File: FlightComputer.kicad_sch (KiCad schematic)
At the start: 0 parts

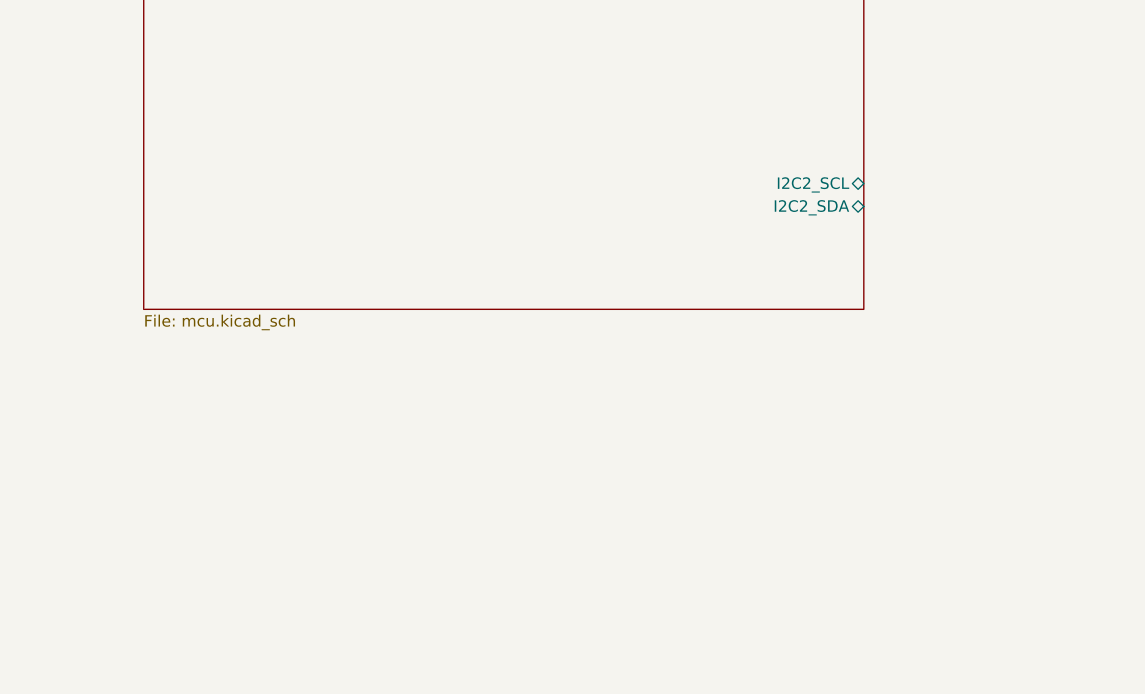
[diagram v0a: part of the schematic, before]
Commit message: Add NavBoard connector and fix Ferrite bead for 3V3A line
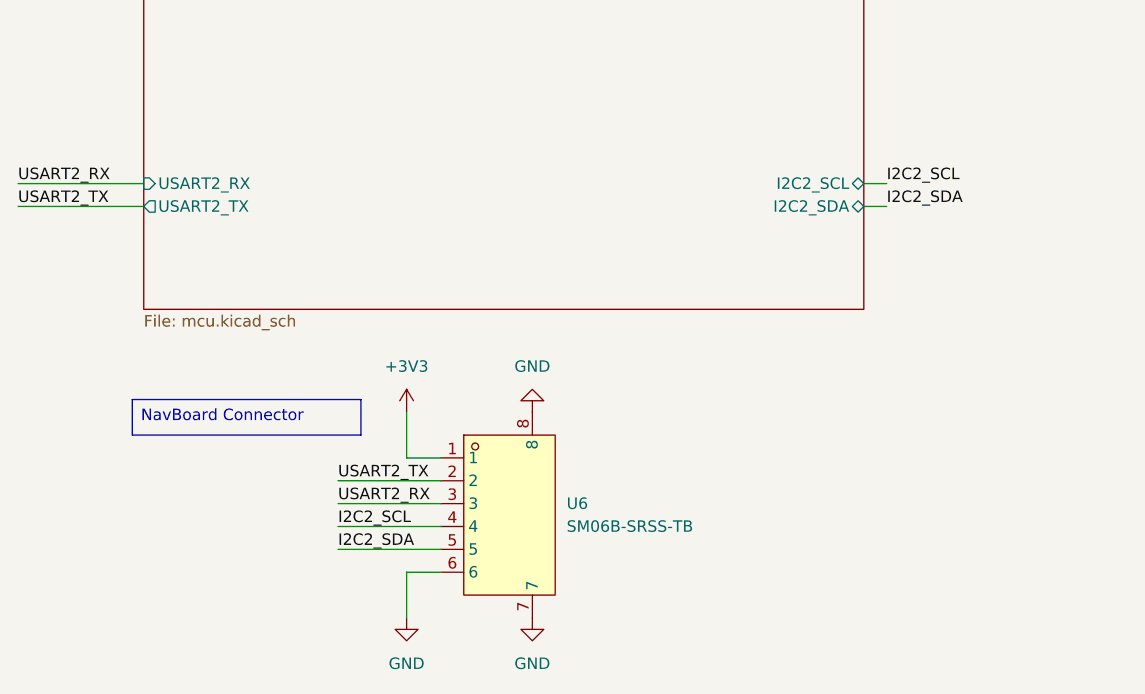
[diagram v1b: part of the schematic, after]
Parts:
- added U6: SM06B-SRSS-TB, LCSC:CONN-SMD_SM06B-SRSS-TB-LF-SN, symbol LCSC:SM06B-SRSS-TB
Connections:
- new net +3V3: U6.1
- new net GND: U6.6, U6.7, U6.8
- new net I2C2_SCL: U6.4
- new net I2C2_SDA: U6.5
- new net USART2_RX: U6.3
- new net USART2_TX: U6.2
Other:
- sheet Microcontroller ports: added USART2_RX, USART2_TX; removed none

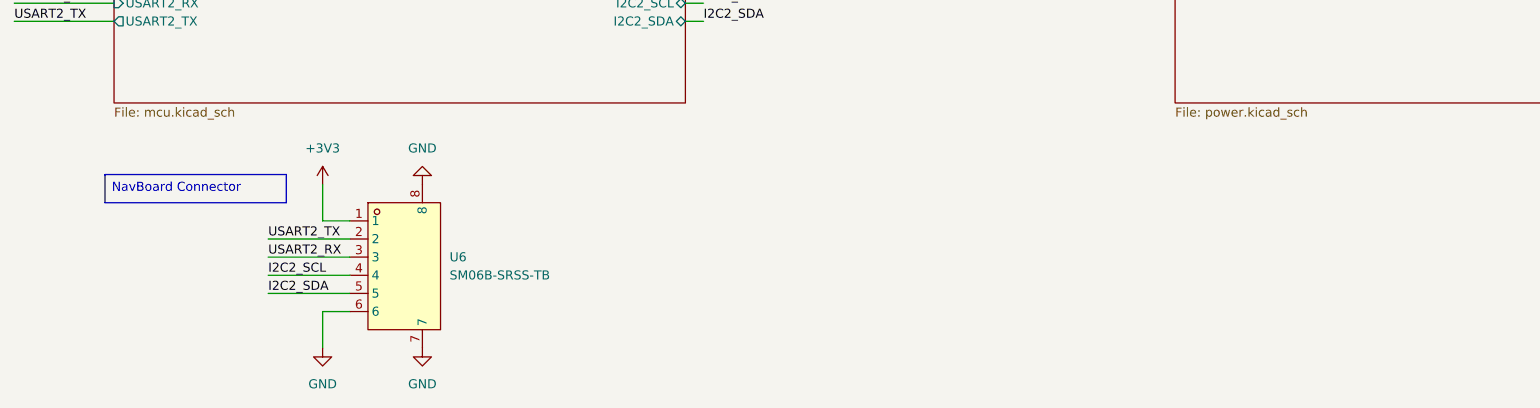
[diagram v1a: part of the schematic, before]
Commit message: Added new connector types for future connections later
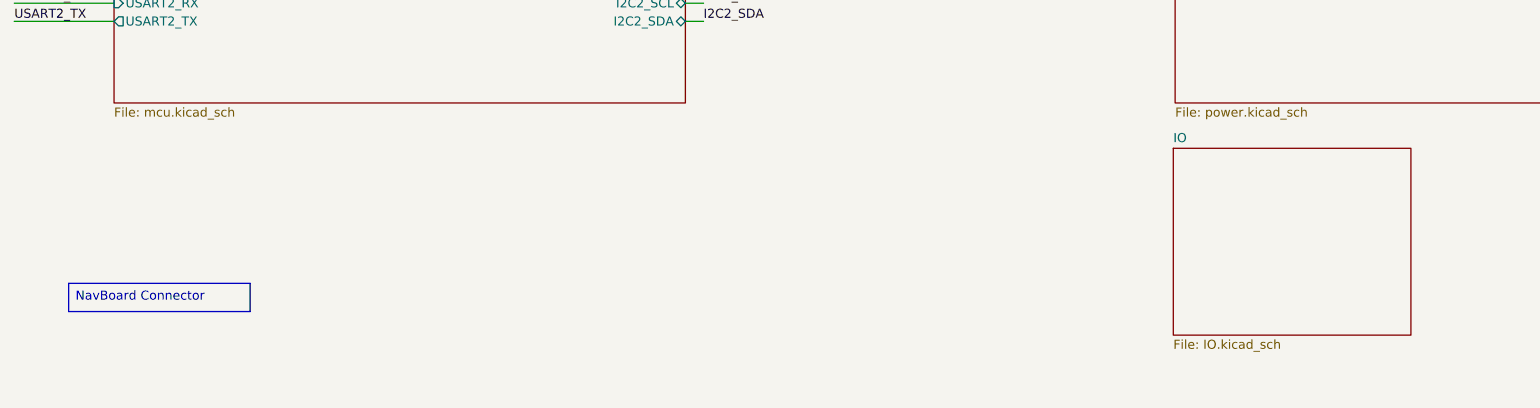
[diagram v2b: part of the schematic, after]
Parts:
- removed U6: SM06B-SRSS-TB, LCSC:CONN-SMD_SM06B-SRSS-TB-LF-SN, symbol LCSC:SM06B-SRSS-TB
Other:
- added sheet IO (IO.kicad_sch)

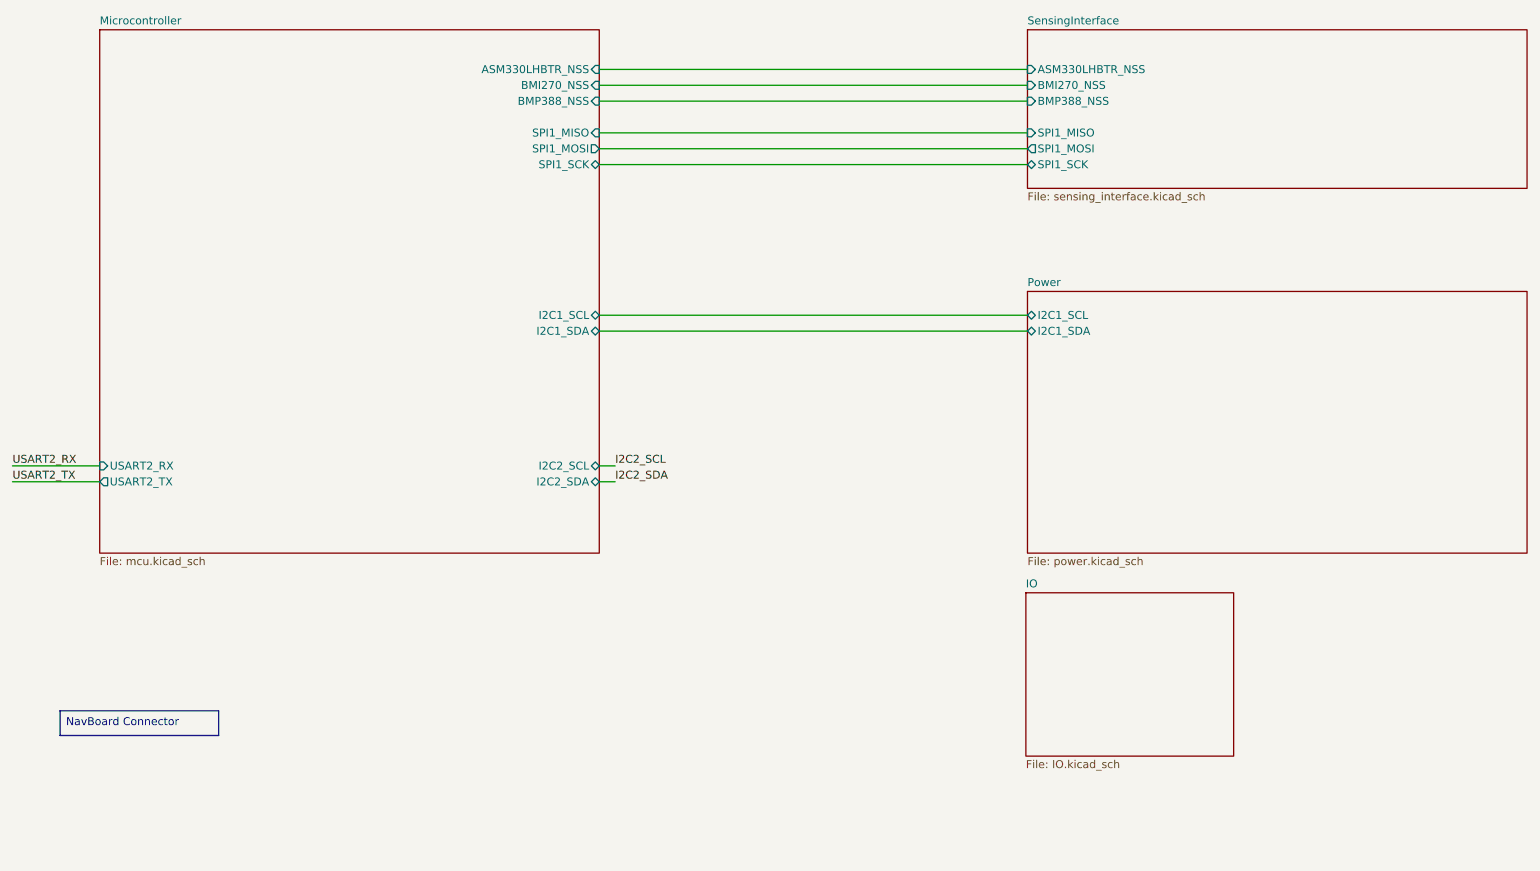
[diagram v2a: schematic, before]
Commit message: mainly added usart 3, uart 4, and I2C3 connections and planning to add a CAN connection
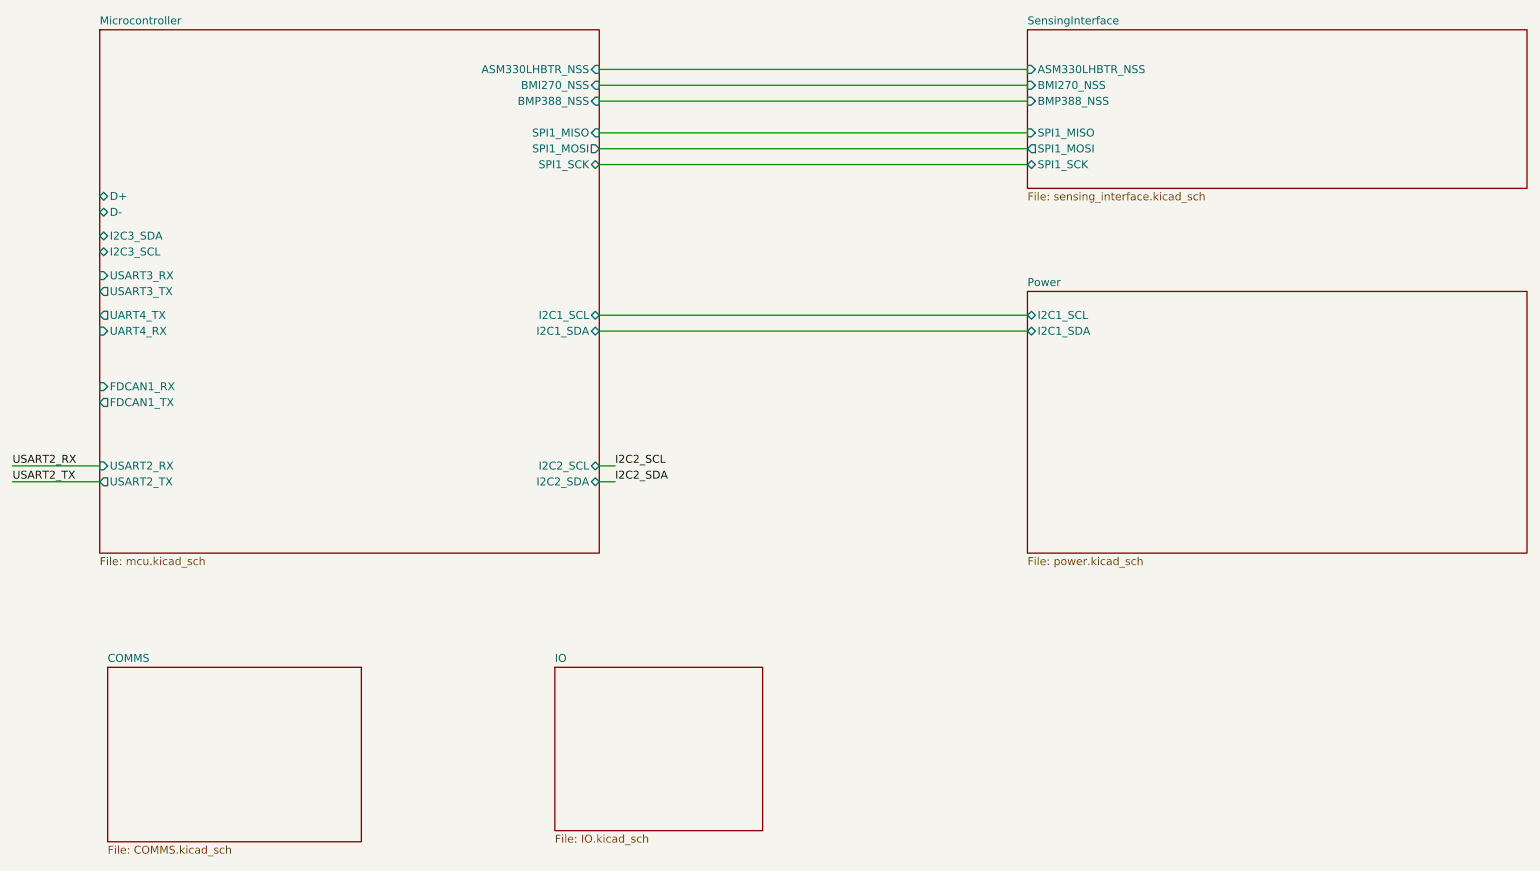
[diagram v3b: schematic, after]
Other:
- added sheet COMMS (COMMS.kicad_sch)
- sheet Microcontroller ports: added D+, D-, FDCAN1_RX, FDCAN1_TX, I2C3_SCL, I2C3_SDA, UART4_RX, UART4_TX, USART3_RX, USART3_TX; removed none
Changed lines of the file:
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@@
 	(generator_version "10.0")
 	(paper "A4")
-	(text_box "NavBoard Connector"
-		(exclude_from_sim no)
-		(at 26.67 153.5317 0)
-		(size 25.4 3.9483)
-		(margins 0.9525 0.9525 0.9525 0.9525)
-		(stroke
-			(width 0)
-			(type solid)
-		)
-		(fill
-			(type none)
-		)
-		(effects
-			(font
-				(size 1.27 1.27)
-			)
-			(justify left top)
-		)
-	)
 	(wire
 		(pts
@@
 			)
 		)
+		(pin "FDCAN1_RX" input
+			(at 33.02 101.6 180)
+			(effects
+				(font
+					(size 1.27 1.27)
+				)
+				(justify left)
+			)
+		)
+		(pin "FDCAN1_TX" output
+			(at 33.02 104.14 180)
+			(effects
+				(font
+					(size 1.27 1.27)
+				)
+				(justify left)
+			)
+		)
+		(pin "I2C3_SCL" bidirectional
+			(at 33.02 80.01 180)
+			(effects
+				(font
+					(size 1.27 1.27)
+				)
+				(justify left)
+			)
+		)
+		(pin "I2C3_SDA" bidirectional
+			(at 33.02 77.47 180)
+			(effects
+				(font
+					(size 1.27 1.27)
+				)
+				(justify left)
+			)
+		)
+		(pin "UART4_RX" input
+			(at 33.02 92.71 180)
+			(effects
+				(font
+					(size 1.27 1.27)
+				)
+				(justify left)
+			)
+		)
+		(pin "UART4_TX" output
+			(at 33.02 90.17 180)
+			(effects
+				(font
+					(size 1.27 1.27)
+				)
+				(justify left)
+			)
+		)
+		(pin "USART3_RX" input
+			(at 33.02 83.82 180)
+			(effects
+				(font
+					(size 1.27 1.27)
+				)
+				(justify left)
+			)
+		)
+		(pin "USART3_TX" output
+			(at 33.02 86.36 180)
+			(effects
+				(font
+					(size 1.27 1.27)
+				)
+				(justify left)
+			)
+		)
+		(pin "D+" bidirectional
+			(at 33.02 71.12 180)
+			(effects
+				(font
+					(size 1.27 1.27)
+				)
+				(justify left)
+			)
+		)
+		(pin "D-" bidirectional
+			(at 33.02 73.66 180)
+			(effects
+				(font
+					(size 1.27 1.27)
+				)
+				(justify left)
+			)
+		)
 		(instances
 			(project "FlightComputer"
@@
 	)
 	(sheet
-		(at 181.356 134.62)
+		(at 105.918 146.558)
 		(size 33.274 26.162)
 		(exclude_from_sim no)
@@
 		)
 		(property "Sheetname" "IO"
-			(at 181.356 133.9084 0)
+			(at 105.918 145.8464 0)
 			(show_name no)
 			(do_not_autoplace no)
@@
 		)
 		(property "Sheetfile" "IO.kicad_sch"
-			(at 181.356 161.3666 0)
+			(at 105.918 173.3046 0)
 			(show_name no)
 			(do_not_autoplace no)
@@
 				)
 			)
+		)
+	)
+	(sheet
+		(at 34.29 146.558)
+		(size 40.64 27.94)
+		(exclude_from_sim no)
+		(in_bom yes)
+		(on_board yes)
+		(dnp no)
+		(fields_autoplaced yes)
+		(stroke
+			(width 0.1524)
+			(type solid)
+		)
+		(fill
+			(color 0 0 0 0)
+		)
+		(property "Sheetname" "COMMS"
+			(at 34.29 145.8464 0)
+			(show_name no)
+			(do_not_autoplace no)
+			(effects
+				(font
+					(size 1.27 1.27)
+				)
+				(justify left bottom)
+			)
+		)
+		(property "Sheetfile" "COMMS.kicad_sch"
+			(at 34.29 175.0826 0)
+			(show_name no)
+			(do_not_autoplace no)
+			(effects
+				(font
+					(size 1.27 1.27)
+				)
+				(justify left top)
+			)
+		)
+		(instances
+			(project "FlightComputer"
+				(path "/c0a97758-75a3-49d0-abcc-edce55d99095"
+					(page "6")
+				)
+			)
